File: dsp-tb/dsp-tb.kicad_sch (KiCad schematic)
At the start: 24 parts, among them J10 USB_C_Receptacle_USB2.0, J2 Conn_ARM_SWD_TagConnect_TC2030, J3 Conn_01x04, J4 Conn_01x04, J5 Conn_01x03, J6 Conn_01x03, J7 Conn_01x03, J8 Conn_01x03, J9 104031-0811, U1 STM32H723ZGTx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

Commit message: dsp-tb: start to include external components for mcu
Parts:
- removed D1, D2, D3: LED, symbol Device:LED
- removed J2: Conn_ARM_SWD_TagConnect_TC2030, Connector:Tag-Connect_TC2030-IDC-FP_2x03_P1.27mm_Vertical, symbol Connector:Conn_ARM_SWD_TagConnect_TC2030
- removed J9: 104031-0811, footprints:MOLEX_104031-0811, symbol MOLEX_104031-0811:104031-0811
- removed U1: STM32H723ZGTx, Package_QFP:LQFP-144_20x20mm_P0.5mm, symbol MCU_ST_STM32H7:STM32H723ZGTx
- removed U5: D3V3XA4B10LP, Package_DFN_QFN:Diodes_UDFN-10_1.0x2.5mm_P0.5mm, symbol Power_Protection:D3V3XA4B10LP
- removed U6: IS42S16800F-7BL-TR, footprints:BGA54C80P9X9_800X800X120, symbol IS42S16800F-7BL-TR:IS42S16800F-7BL-TR
- removed U7: IS25LP080D-JNLE, footprints:SOIC127P600X88-8N, symbol IS25LP080D-JNLE:IS25LP080D-JNLE
- J3, J4: footprint (none) -> Connector_Molex:Molex_PicoBlade_53048-0410_1x04_P1.25mm_Horizontal
- J5, J6, J7, J8: footprint (none) -> Connector_Molex:Molex_PicoBlade_53048-0310_1x03_P1.25mm_Horizontal
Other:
- added sheet MCU (mcu.kicad_sch)
- added sheet MEMORY (memory.kicad_sch)
- note removed: "Memory"
- note removed: "Programming Header"
- note removed: "Status Indicators and Control"
- note removed: "TO DO: - include GPIO switches"
- note removed: "x4 VDDQ pins x3 VDD pins"

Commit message: dsp-tb: sch: small arrangement changes
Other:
- note removed: "MCU"
- moved on the sheet: J10, J3, J4, J5, J6, J7, J8, U10, U11, U12, U13, U14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

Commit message: dsp: boot0 and reset switches
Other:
- moved on the sheet: U8
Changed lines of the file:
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@@
     )
   )
-  (symbol (lib_id "USB3318C-CP-TR:USB3318C-CP-TR") (at 170.18 123.19 0) (unit 1)
+  (symbol (lib_id "USB3318C-CP-TR:USB3318C-CP-TR") (at 118.11 123.19 0) (unit 1)
     (in_bom yes) (on_board yes) (dnp no) (fields_autoplaced)
-    (property "Reference" "U8" (at 205.74 114.3 0)
+    (property "Reference" "U8" (at 153.67 114.3 0)
       (effects (font (size 1.524 1.524)))
     )
-    (property "Value" "USB3318C-CP-TR" (at 205.74 116.84 0)
+    (property "Value" "USB3318C-CP-TR" (at 153.67 116.84 0)
       (effects (font (size 1.524 1.524)))
     )
-    (property "Footprint" "footprints:QFN24_4X4MC_MCH" (at 170.18 123.19 0)
+    (property "Footprint" "footprints:QFN24_4X4MC_MCH" (at 118.11 123.19 0)
       (effects (font (size 1.27 1.27) italic) hide)
     )
-    (property "Datasheet" "USB3318C-CP-TR" (at 170.18 123.19 0)
+    (property "Datasheet" "USB3318C-CP-TR" (at 118.11 123.19 0)
       (effects (font (size 1.27 1.27) italic) hide)
     )

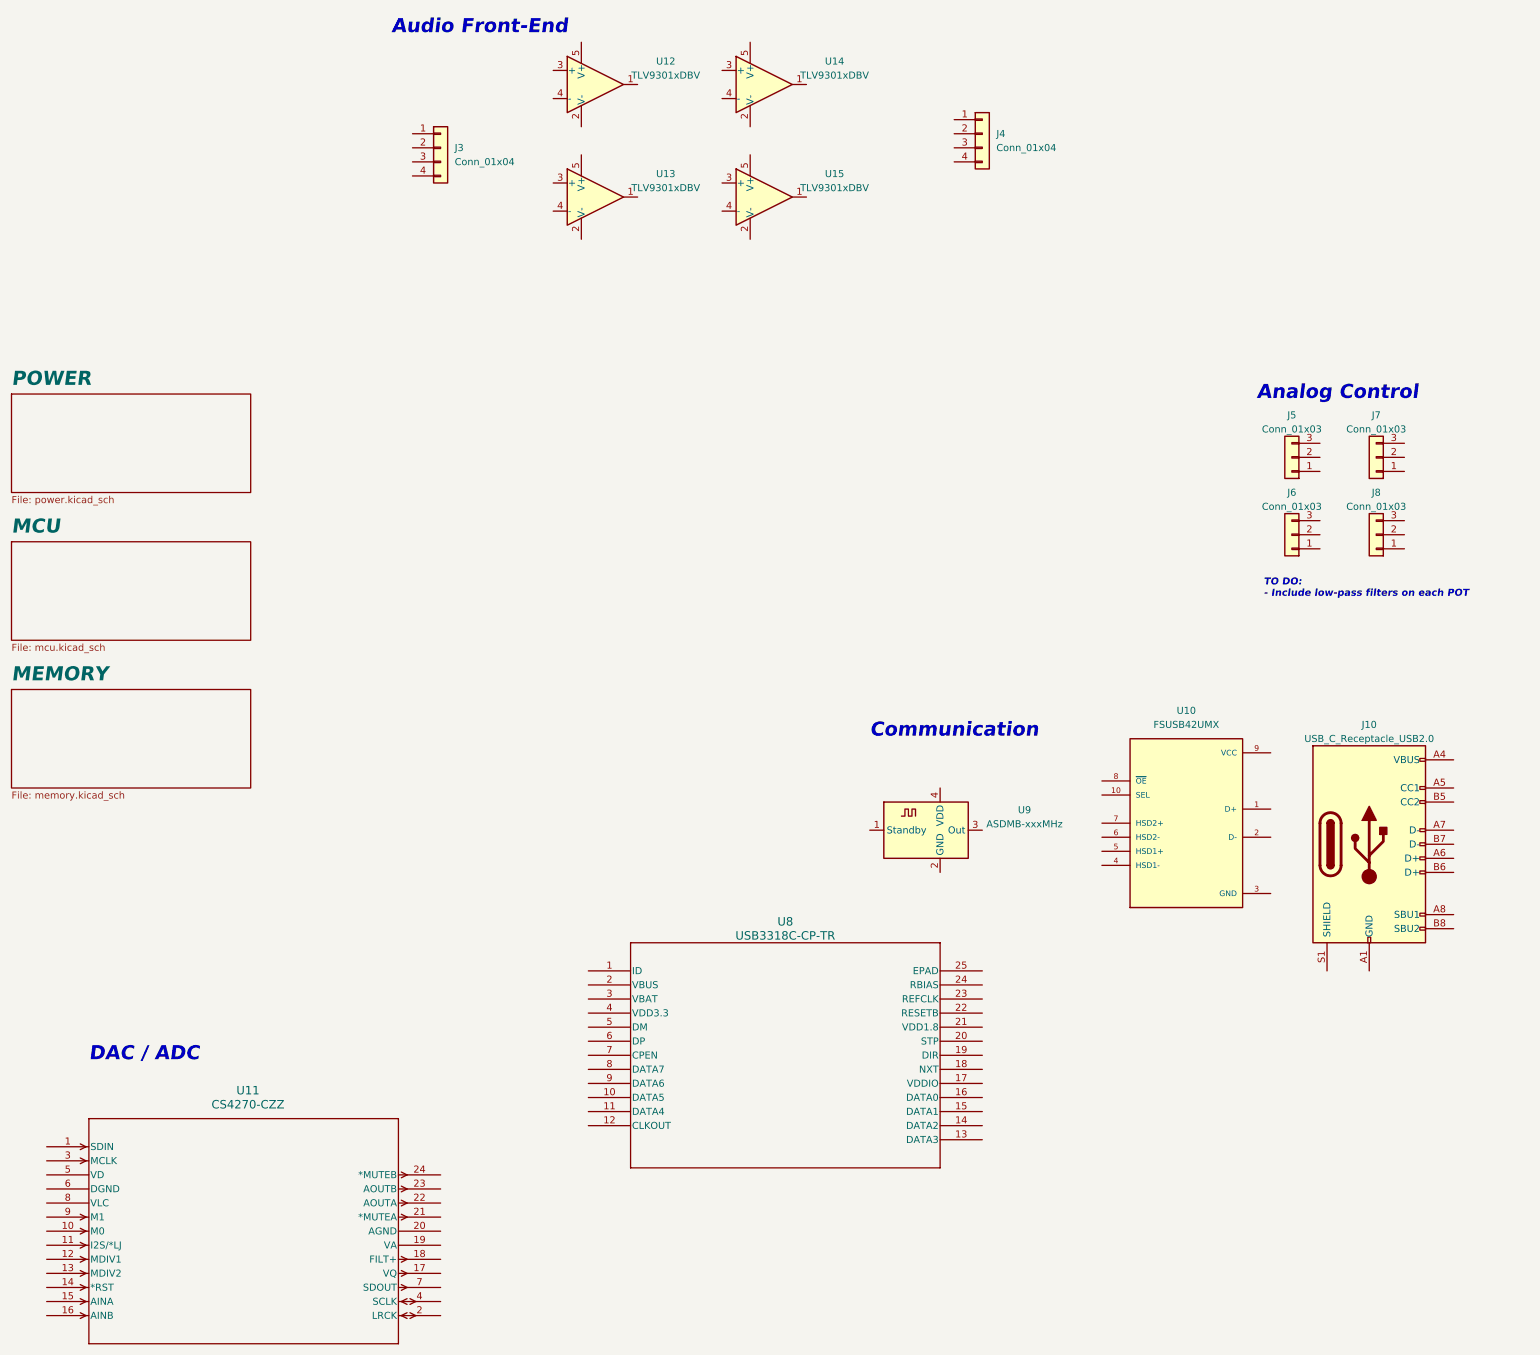
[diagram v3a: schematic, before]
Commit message: dsp-tb: finish schematic drawings
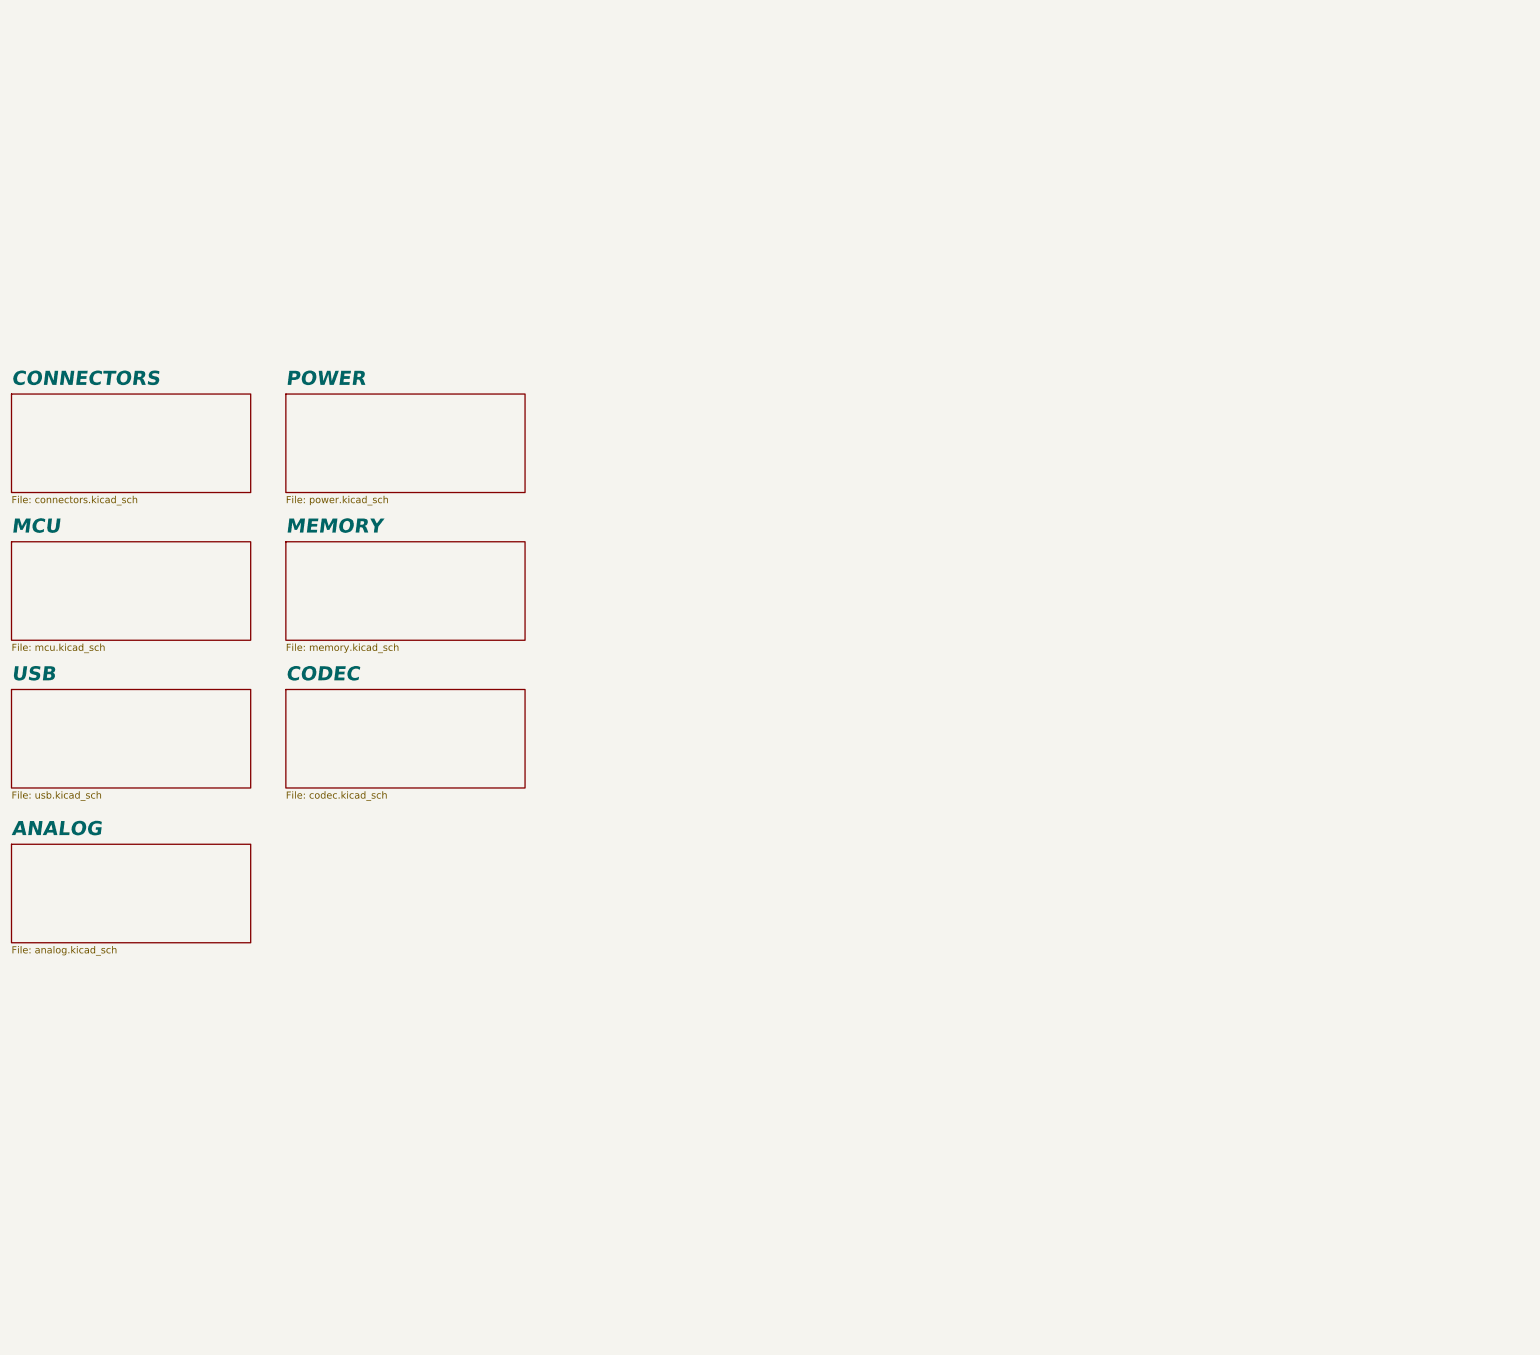
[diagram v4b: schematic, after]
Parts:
- removed J10: USB_C_Receptacle_USB2.0, Connector_USB:USB_C_Receptacle_GCT_USB4085, symbol Connector:USB_C_Receptacle_USB2.0
- removed J3, J4: Conn_01x04, Connector_Molex:Molex_PicoBlade_53048-0410_1x04_P1.25mm_Horizontal, symbol Connector_Generic:Conn_01x04
- removed J5, J6, J7, J8: Conn_01x03, Connector_Molex:Molex_PicoBlade_53048-0310_1x03_P1.25mm_Horizontal, symbol Connector_Generic:Conn_01x03
- removed U10: FSUSB42UMX, footprints:IC_FSUSB42UMX, symbol FSUSB42UMX:FSUSB42UMX
- removed U11: CS4270-CZZ, footprints:codec-cs4270, symbol codec-cs4270:CS4270-CZZ
- removed U12, U13, U14, U15: TLV9301xDBV, Package_TO_SOT_SMD:SOT-23-5, symbol Amplifier_Operational:TLV9301xDBV
- removed U8: USB3318C-CP-TR, footprints:QFN24_4X4MC_MCH, symbol USB3318C-CP-TR:USB3318C-CP-TR
- removed U9: ASDMB-xxxMHz, Oscillator:Oscillator_SMD_Abracon_ASDMB-4Pin_2.5x2.0mm, symbol Oscillator:ASDMB-xxxMHz
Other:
- added sheet ANALOG (analog.kicad_sch)
- added sheet CODEC (codec.kicad_sch)
- added sheet CONNECTORS (connectors.kicad_sch)
- added sheet USB (usb.kicad_sch)
- note removed: "Analog Control"
- note removed: "Audio Front-End"
- note removed: "Communication"
- note removed: "DAC / ADC"
- note removed: "TO DO: - Include low-pass filters on each POT"
